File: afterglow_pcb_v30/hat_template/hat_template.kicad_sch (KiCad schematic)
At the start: 4 parts, among them J4 Conn_01x10_Pin, J5 Conn_01x10_Pin, J7 Conn_02x03_Odd_Even, J8 Conn_02x03_Odd_Even

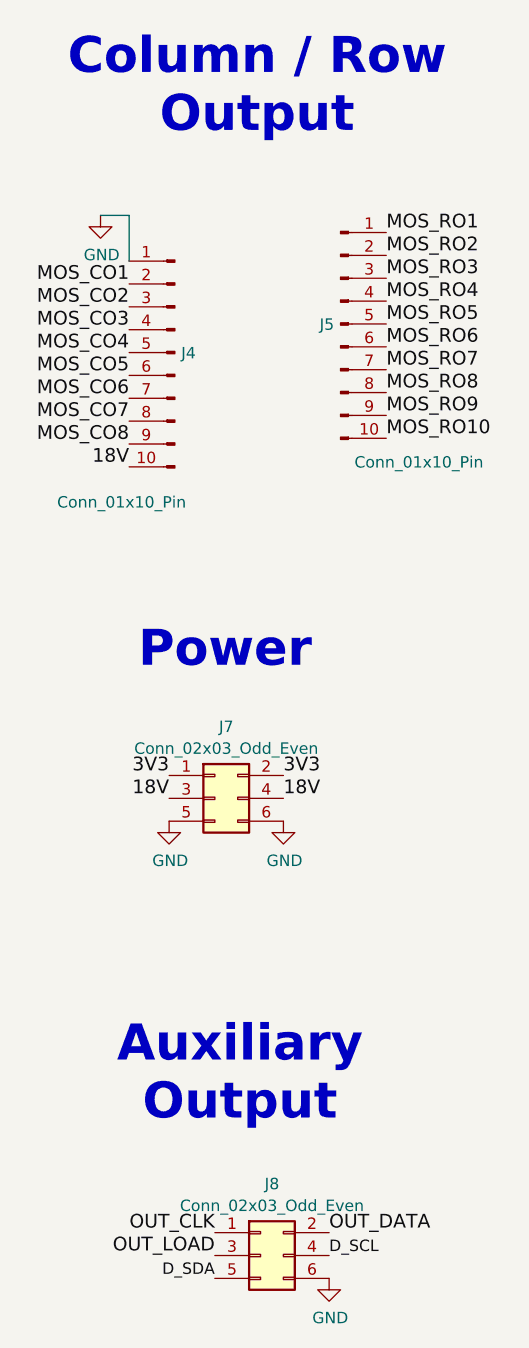
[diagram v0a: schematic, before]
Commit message: Hat i2c pinout fix
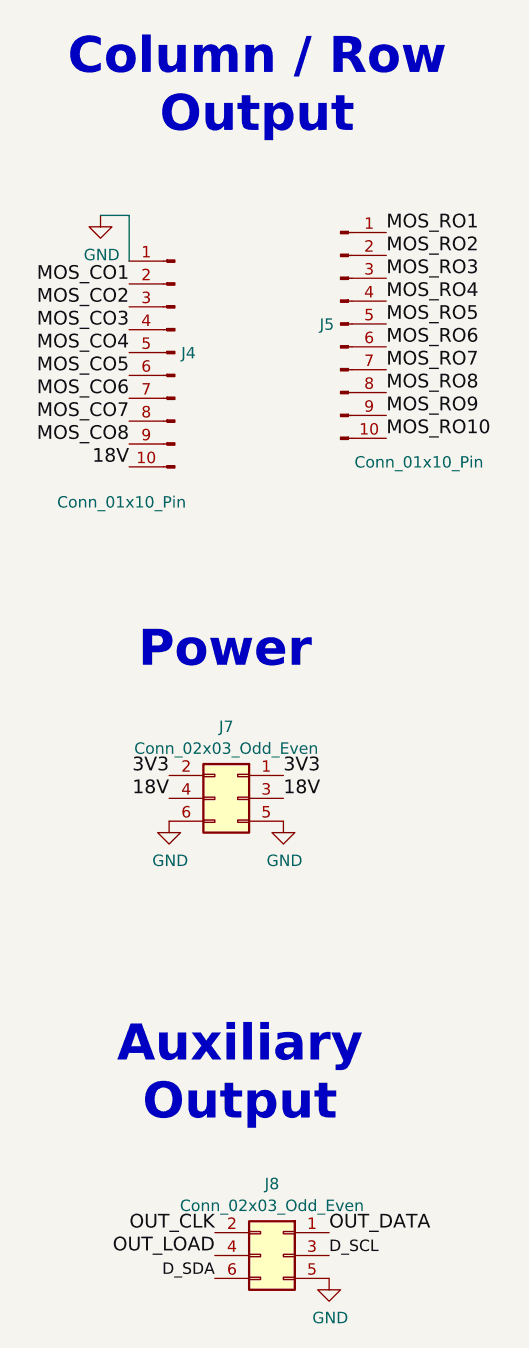
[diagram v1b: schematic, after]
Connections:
- net D_SCL: now also J8.3 (Pin_3); no longer J8.4 (Pin_4)
- net D_SDA: now also J8.6 (Pin_6); no longer J8.5 (Pin_5)
- net GND: now also J8.5 (Pin_5); no longer J8.6 (Pin_6)
- net OUT_CLK: now also J8.2 (Pin_2); no longer J8.1 (Pin_1)
- net OUT_DATA: now also J8.1 (Pin_1); no longer J8.2 (Pin_2)
- net OUT_LOAD: now also J8.4 (Pin_4); no longer J8.3 (Pin_3)
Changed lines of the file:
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@@
 		)
 		(instances
-			(project "afterglow_pcb_v30_hat_template"
+			(project "hat_template"
 				(path "/86dc7a78-7d51-4111-9eea-8a8f7977eb16"
 					(reference "#PWR033")
@@
 		)
 		(instances
-			(project "afterglow_pcb_v30_hat_template"
+			(project "hat_template"
 				(path "/86dc7a78-7d51-4111-9eea-8a8f7977eb16"
 					(reference "#PWR035")
@@
 		)
 		(instances
-			(project "afterglow_pcb_v30_hat_template"
+			(project "hat_template"
 				(path "/86dc7a78-7d51-4111-9eea-8a8f7977eb16"
 					(reference "J4")
@@
 		)
 		(instances
-			(project "afterglow_pcb_v30_hat_template"
+			(project "hat_template"
 				(path "/86dc7a78-7d51-4111-9eea-8a8f7977eb16"
 					(reference "#PWR028")
@@
 	(symbol
 		(lib_id "Connector_Generic:Conn_02x03_Odd_Even")
-		(at 52.705 164.465 0)
+		(at 55.245 164.465 0)
+		(mirror y)
 		(unit 1)
 		(exclude_from_sim no)
@@
 		)
 		(property "Footprint" "Connector_PinHeader_2.54mm:PinHeader_2x03_P2.54mm_Vertical"
-			(at 52.705 164.465 0)
+			(at 55.245 164.465 0)
 			(effects
 				(font
@@
 		)
 		(property "Datasheet" "~"
-			(at 52.705 164.465 0)
-			(effects
-				(font
-					(size 1.27 1.27)
-				)
-				(hide yes)
-			)
-		)
-		(property "Description" ""
-			(at 52.705 164.465 0)
+			(at 55.245 164.465 0)
+			(effects
+				(font
+					(size 1.27 1.27)
+				)
+				(hide yes)
+			)
+		)
+		(property "Description" ""
+			(at 55.245 164.465 0)
 			(effects
 				(font
@@
 		)
 		(property "JLCPCB" "C92272"
-			(at 52.705 164.465 0)
+			(at 55.245 164.465 0)
 			(effects
 				(font
@@
 		)
 		(instances
-			(project "afterglow_pcb_v30_hat_template"
+			(project "hat_template"
 				(path "/86dc7a78-7d51-4111-9eea-8a8f7977eb16"
 					(reference "J8")
@@
 		)
 		(instances
-			(project "afterglow_pcb_v30_hat_template"
+			(project "hat_template"
 				(path "/86dc7a78-7d51-4111-9eea-8a8f7977eb16"
 					(reference "J5")
@@
 	(symbol
 		(lib_id "Connector_Generic:Conn_02x03_Odd_Even")
-		(at 47.625 113.665 0)
+		(at 50.165 113.665 0)
+		(mirror y)
 		(unit 1)
 		(exclude_from_sim no)
@@
 		)
 		(property "Footprint" "Connector_PinHeader_2.54mm:PinHeader_2x03_P2.54mm_Vertical"
-			(at 47.625 113.665 0)
+			(at 50.165 113.665 0)
 			(effects
 				(font
@@
 		)
 		(property "Datasheet" "~"
-			(at 47.625 113.665 0)
-			(effects
-				(font
-					(size 1.27 1.27)
-				)
-				(hide yes)
-			)
-		)
-		(property "Description" ""
-			(at 47.625 113.665 0)
+			(at 50.165 113.665 0)
+			(effects
+				(font
+					(size 1.27 1.27)
+				)
+				(hide yes)
+			)
+		)
+		(property "Description" ""
+			(at 50.165 113.665 0)
 			(effects
 				(font
@@
 		)
 		(property "JLCPCB" "C92272"
-			(at 47.625 113.665 0)
+			(at 50.165 113.665 0)
 			(effects
 				(font
@@
 		)
 		(instances
-			(project "afterglow_pcb_v30_hat_template"
+			(project "hat_template"
 				(path "/86dc7a78-7d51-4111-9eea-8a8f7977eb16"
 					(reference "J7")
@@
 		)
 		(instances
-			(project "afterglow_pcb_v30_hat_template"
+			(project "hat_template"
 				(path "/86dc7a78-7d51-4111-9eea-8a8f7977eb16"
 					(reference "#PWR036")
